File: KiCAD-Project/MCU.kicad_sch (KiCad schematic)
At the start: 35 parts, among them J301 GPIOs, J302 JTAG/SWD, J303 Conn_01x03_Shielded, U301 CY8C6244AZI-S4D92, U302 MCP9700AT-HTT, Y301 32MHz

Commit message: fixing DRC
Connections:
- net DRV_CAL: now also U301.43 (P9.4); no longer U301.48 (P10.0)
- net DRV_CS: now also U301.42 (P9.3); no longer U301.36 (P7.3)
- net DRV_MISO: now also U301.40 (P9.1); no longer U301.38 (P8.1)
- net DRV_MOSI: now also U301.39 (P9.0); no longer U301.37 (P8.0)
- net DRV_PWM_AH: now also U301.34 (P7.1); no longer U301.40 (P9.1)
- net DRV_PWM_AL: now also U301.33 (P7.0); no longer U301.39 (P9.0)
- net DRV_PWM_BH: now also U301.36 (P7.3); no longer U301.42 (P9.3)
- net DRV_PWM_BL: now also U301.35 (P7.2); no longer U301.41 (P9.2)
- net DRV_PWM_CH: now also U301.38 (P8.1); no longer U301.44 (P9.5)
- net DRV_PWM_CL: now also U301.37 (P8.0); no longer U301.43 (P9.4)
- net DRV_SCK: now also U301.41 (P9.2); no longer U301.35 (P7.2)
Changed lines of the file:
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@@
   (no_connect (at 158.75 27.94))
   (no_connect (at 158.75 33.02))
-  (no_connect (at 158.75 43.18))
-  (no_connect (at 158.75 45.72))
+  (no_connect (at 158.75 78.74))
+  (no_connect (at 158.75 83.82))
   (no_connect (at 158.75 101.6))
   (no_connect (at 339.09 148.59))
@@
     (stroke (width 0) (type solid) (color 0 0 0 0))
   )
+  (wire (pts (xy 158.75 43.18) (xy 193.04 43.18))
+    (stroke (width 0) (type solid) (color 0 0 0 0))
+  )
+  (wire (pts (xy 158.75 45.72) (xy 193.04 45.72))
+    (stroke (width 0) (type solid) (color 0 0 0 0))
+  )
   (wire (pts (xy 158.75 48.26) (xy 193.04 48.26))
     (stroke (width 0) (type solid) (color 0 0 0 0))
@@
   )
   (wire (pts (xy 158.75 76.2) (xy 193.04 76.2))
-    (stroke (width 0) (type solid) (color 0 0 0 0))
-  )
-  (wire (pts (xy 158.75 78.74) (xy 193.04 78.74))
-    (stroke (width 0) (type solid) (color 0 0 0 0))
-  )
-  (wire (pts (xy 158.75 83.82) (xy 193.04 83.82))
     (stroke (width 0) (type solid) (color 0 0 0 0))
   )
@@
     (effects (font (size 1.27 1.27)) (justify right))
   )
-  (hierarchical_label "DRV_SCK" (shape input) (at 193.04 48.26 0)
-    (effects (font (size 1.27 1.27)) (justify left))
-  )
-  (hierarchical_label "DRV_CS" (shape input) (at 193.04 50.8 0)
-    (effects (font (size 1.27 1.27)) (justify left))
-  )
-  (hierarchical_label "DRV_MOSI" (shape input) (at 193.04 58.42 0)
-    (effects (font (size 1.27 1.27)) (justify left))
-  )
-  (hierarchical_label "DRV_MISO" (shape input) (at 193.04 60.96 0)
-    (effects (font (size 1.27 1.27)) (justify left))
-  )
-  (hierarchical_label "DRV_PWM_AL" (shape input) (at 193.04 66.04 0)
-    (effects (font (size 1.27 1.27)) (justify left))
-  )
-  (hierarchical_label "DRV_PWM_AH" (shape input) (at 193.04 68.58 0)
-    (effects (font (size 1.27 1.27)) (justify left))
-  )
-  (hierarchical_label "DRV_PWM_BL" (shape input) (at 193.04 71.12 0)
-    (effects (font (size 1.27 1.27)) (justify left))
-  )
-  (hierarchical_label "DRV_PWM_BH" (shape input) (at 193.04 73.66 0)
-    (effects (font (size 1.27 1.27)) (justify left))
-  )
-  (hierarchical_label "DRV_PWM_CL" (shape input) (at 193.04 76.2 0)
-    (effects (font (size 1.27 1.27)) (justify left))
-  )
-  (hierarchical_label "DRV_PWM_CH" (shape input) (at 193.04 78.74 0)
-    (effects (font (size 1.27 1.27)) (justify left))
-  )
-  (hierarchical_label "DRV_CAL" (shape input) (at 193.04 83.82 0)
-    (effects (font (size 1.27 1.27)) (justify left))
-  )
+  (hierarchical_label "DRV_PWM_AL" (shape input) (at 193.04 43.18 0)
+    (effects (font (size 1.27 1.27)) (justify left))
+  )
+  (hierarchical_label "DRV_PWM_AH" (shape input) (at 193.04 45.72 0)
+    (effects (font (size 1.27 1.27)) (justify left))
+  )
+  (hierarchical_label "DRV_PWM_BL" (shape input) (at 193.04 48.26 0)
+    (effects (font (size 1.27 1.27)) (justify left))
+  )
+  (hierarchical_label "DRV_PWM_BH" (shape input) (at 193.04 50.8 0)
+    (effects (font (size 1.27 1.27)) (justify left))
+  )
+  (hierarchical_label "DRV_PWM_CL" (shape input) (at 193.04 58.42 0)
+    (effects (font (size 1.27 1.27)) (justify left))
+  )
+  (hierarchical_label "DRV_PWM_CH" (shape input) (at 193.04 60.96 0)
+    (effects (font (size 1.27 1.27)) (justify left))
+  )
+  (hierarchical_label "DRV_MOSI" (shape input) (at 193.04 66.04 0)
+    (effects (font (size 1.27 1.27)) (justify left))
+  )
+  (hierarchical_label "DRV_MISO" (shape input) (at 193.04 68.58 0)
+    (effects (font (size 1.27 1.27)) (justify left))
+  )
+  (hierarchical_label "DRV_SCK" (shape input) (at 193.04 71.12 0)
+    (effects (font (size 1.27 1.27)) (justify left))
+  )
+  (hierarchical_label "DRV_CS" (shape input) (at 193.04 73.66 0)
+    (effects (font (size 1.27 1.27)) (justify left))
+  )
+  (hierarchical_label "DRV_CAL" (shape input) (at 193.04 76.2 0)
+    (effects (font (size 1.27 1.27)) (justify left))
+  )

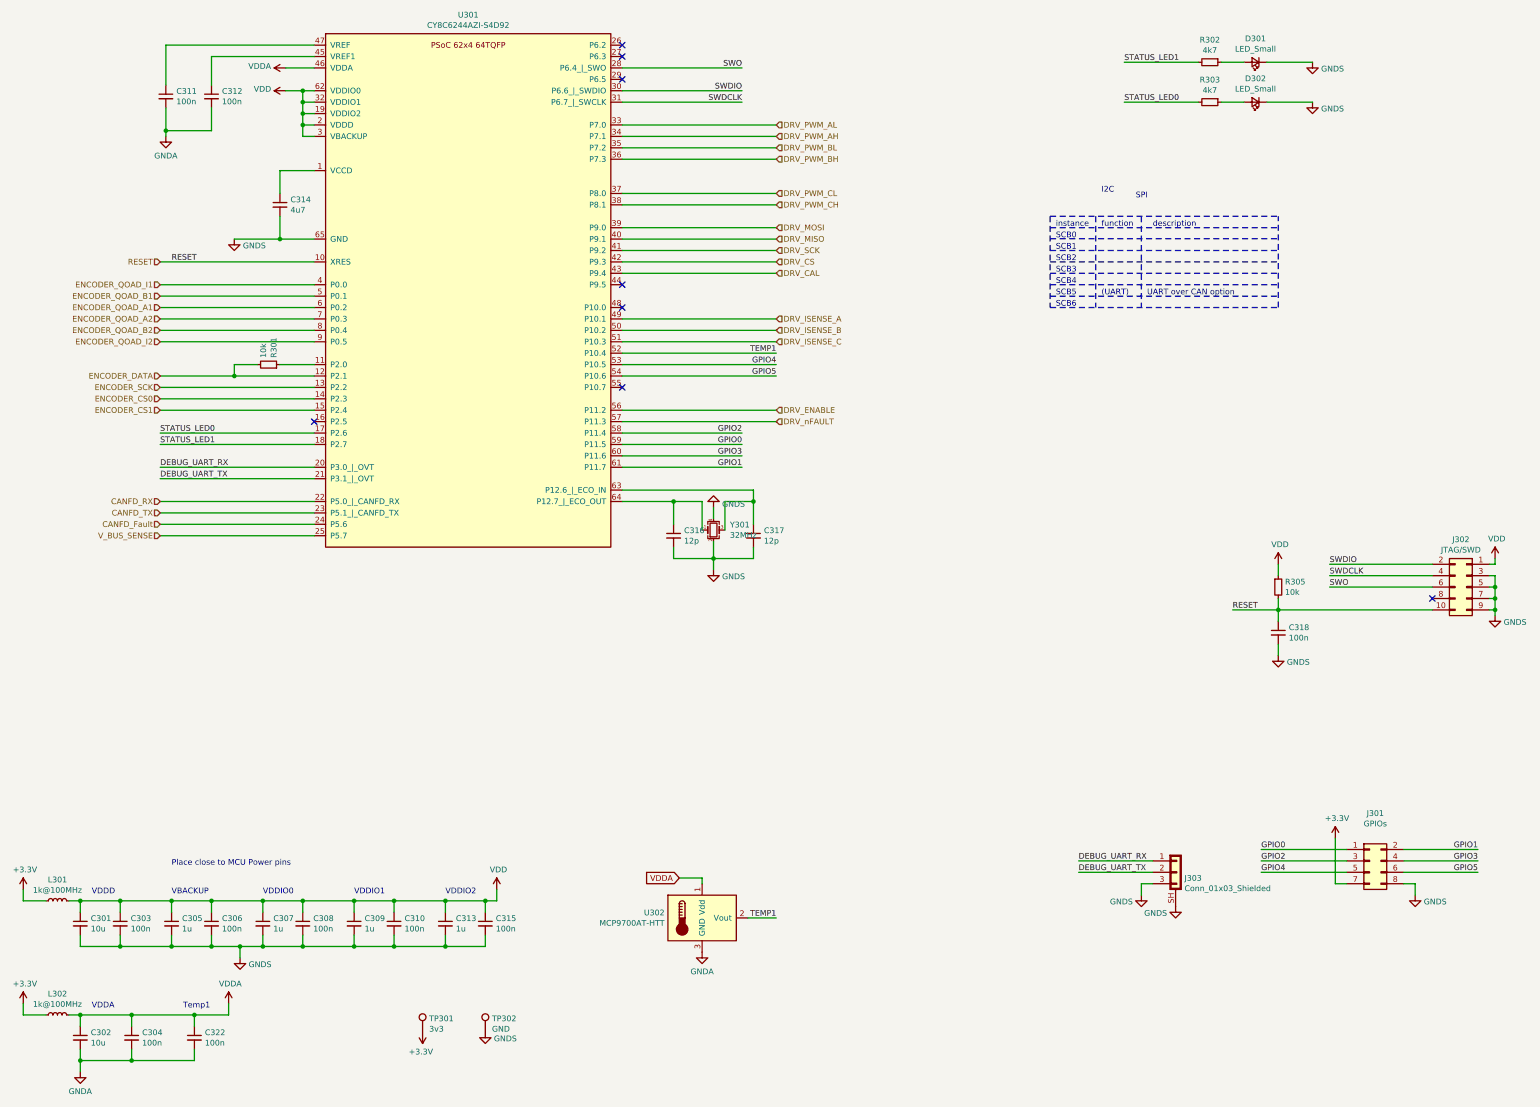
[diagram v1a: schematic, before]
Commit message: DRC resolved
removed GNDA, GNDS from schematic due to no solution was found to get a net-tie in inner layers
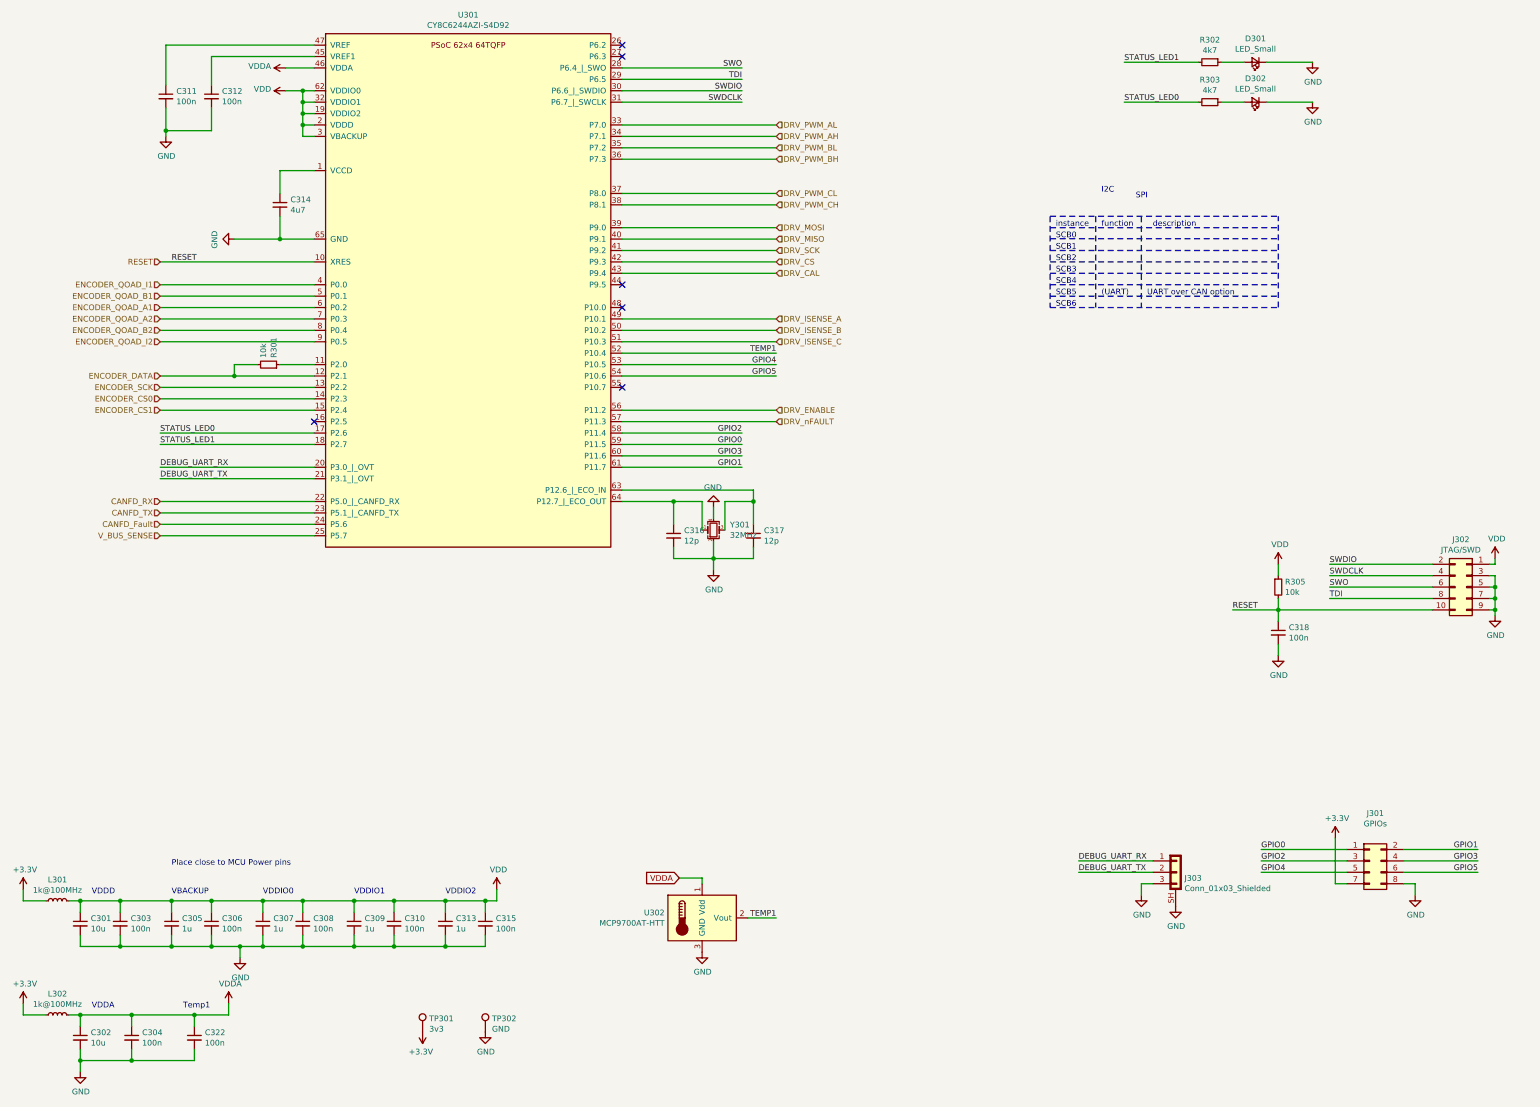
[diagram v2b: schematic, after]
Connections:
- net GNDS is gone; now on net GND: C301.2, C303.2, C305.2, C306.2, C307.2, C308.2, C309.2, C310.2, C313.2, C314.2, C315.2, C316.2, C317.2, C318.2, D301.1 (K), D302.1 (K), J301.8 (Pin_8), J302.3 (Pin_3), J302.5 (Pin_5), J302.7 (Pin_7), J302.9 (Pin_9), J303.3 (Pin_3), J303.SH (Shield), TP302.1, U301.65 (GND), Y301.2, Y301.4
- net TDI: now reaches U301.29 (P6.5)
- net TDI: now also J302.8 (Pin_8)
- net GNDA renamed GND
- no-connect marks 8 -> 6

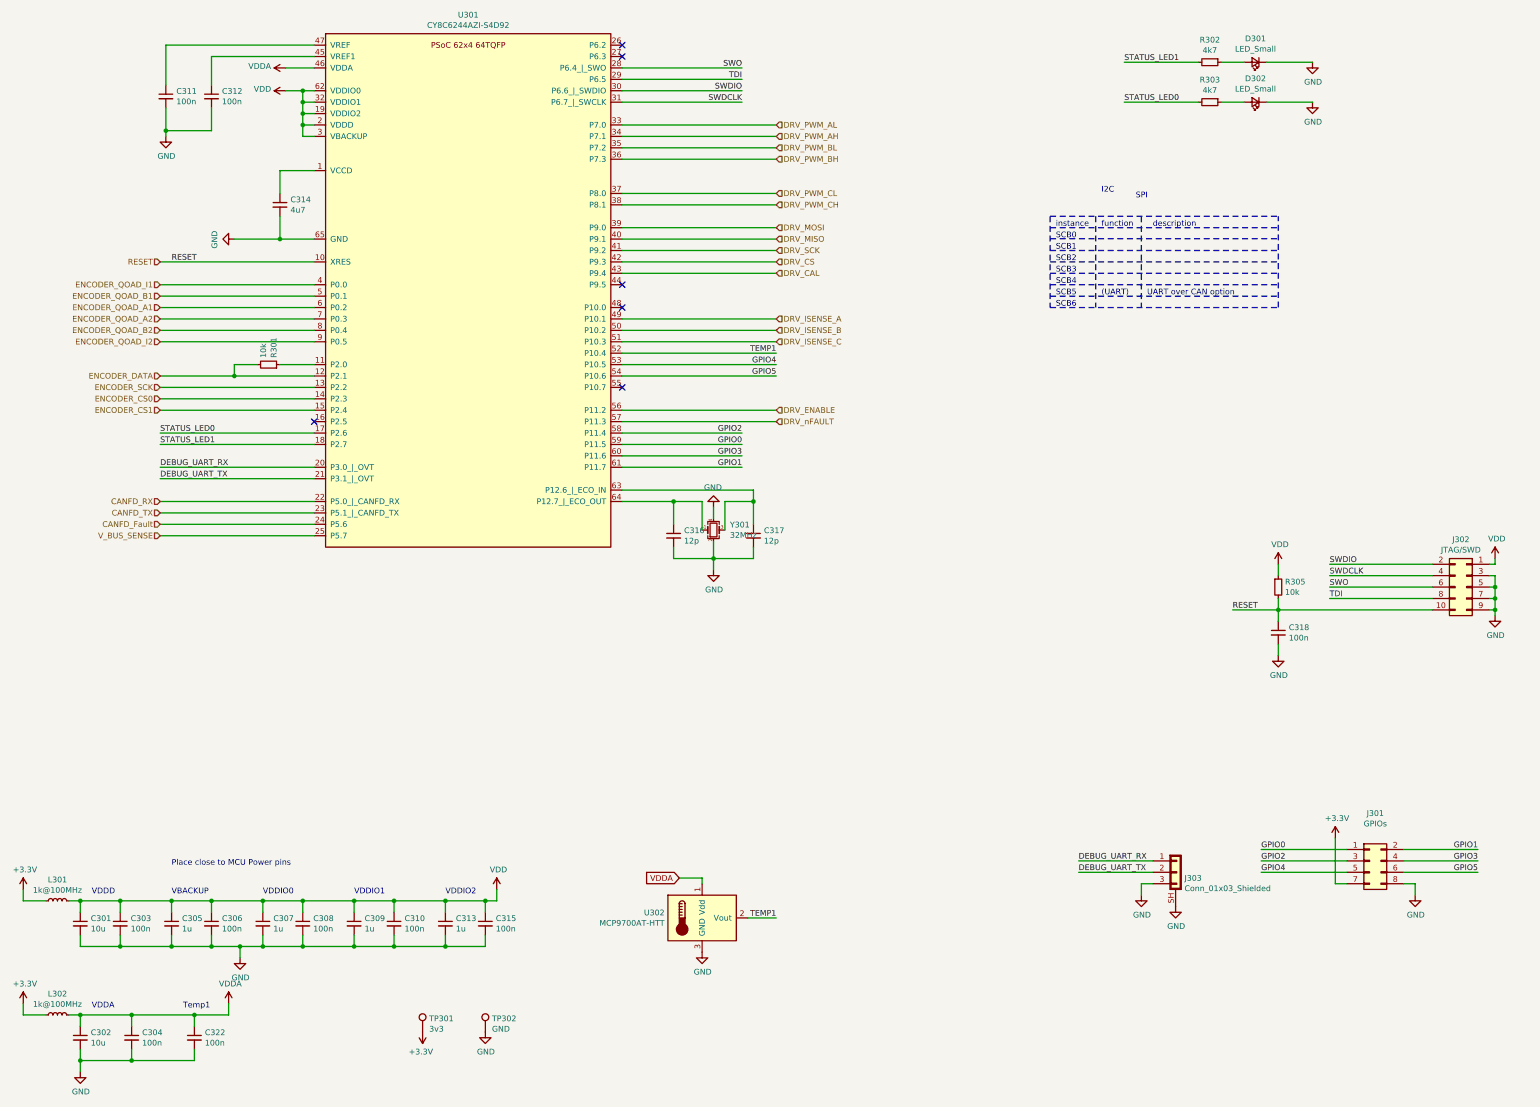
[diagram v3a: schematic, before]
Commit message: assigned debug UART to different pins
debug UART and DRV SPI used same SCB
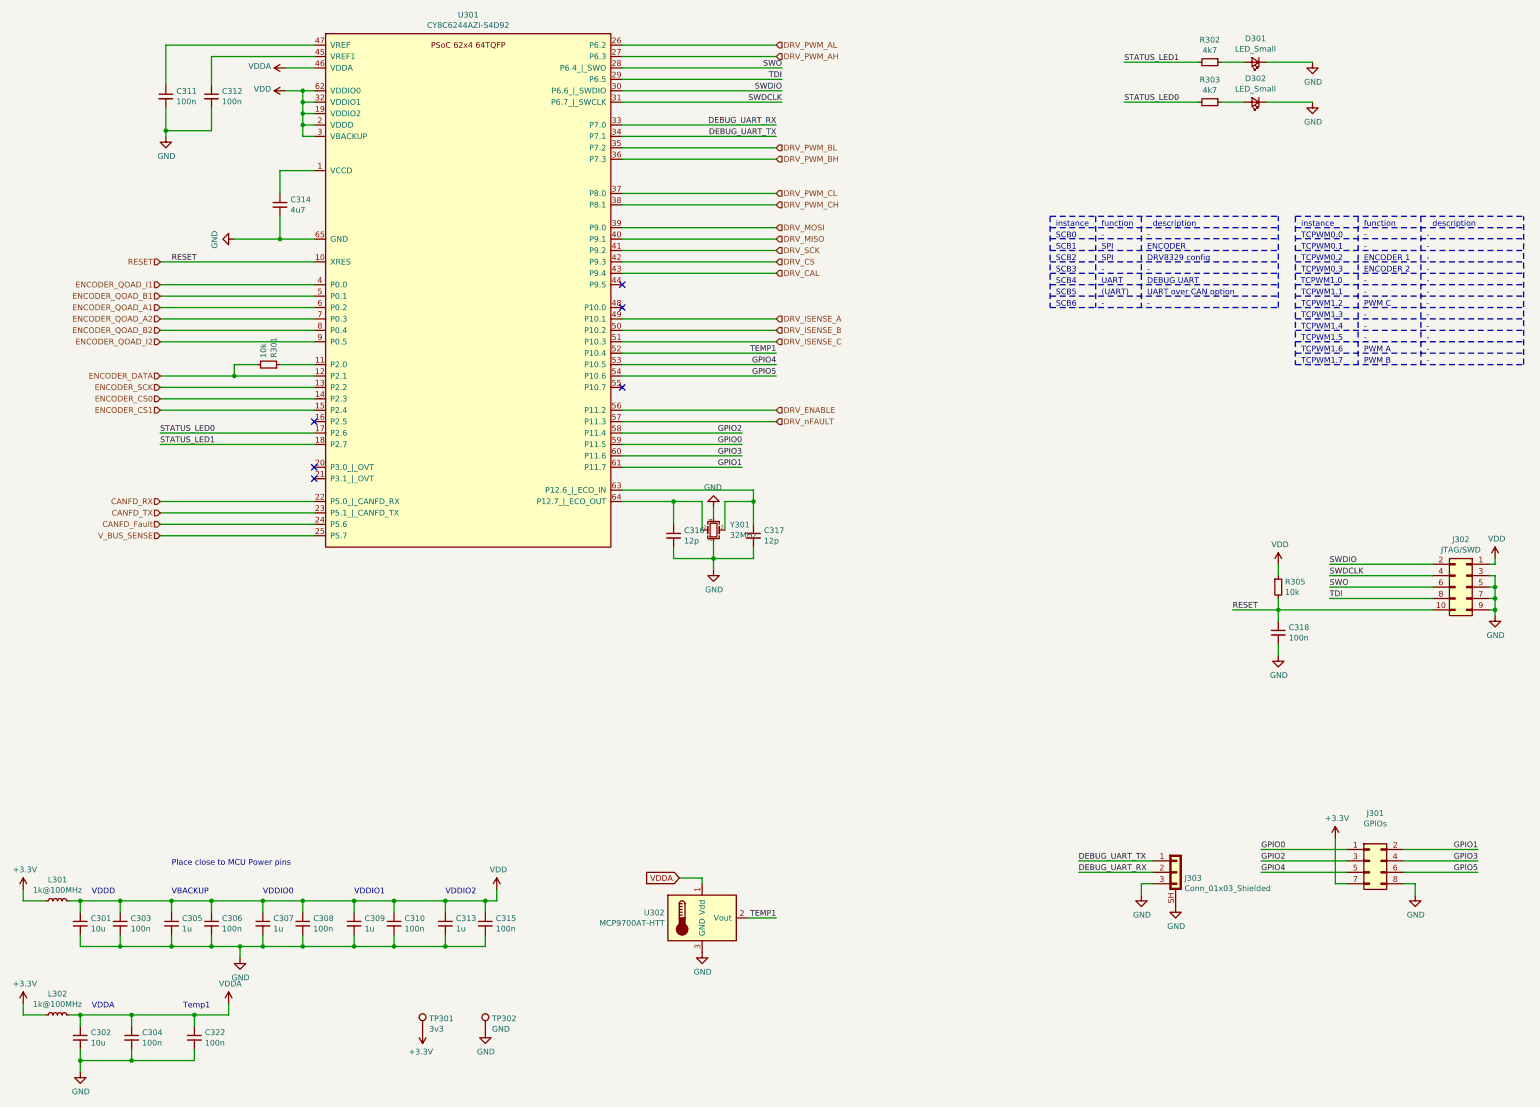
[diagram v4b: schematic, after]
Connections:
- net DEBUG_UART_RX: now also J303.2 (Pin_2), U301.33 (P7.0); no longer J303.1 (Pin_1), U301.20 (P3.0_|_OVT)
- net DEBUG_UART_TX: now also J303.1 (Pin_1), U301.34 (P7.1); no longer J303.2 (Pin_2), U301.21 (P3.1_|_OVT)
- net DRV_PWM_AH: now also U301.27 (P6.3); no longer U301.34 (P7.1)
- net DRV_PWM_AL: now also U301.26 (P6.2); no longer U301.33 (P7.0)
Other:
- note added: "-"
- note added: "DEBUG UART"
- note added: "DRV8329 config"
- note added: "ENCODER"
- note added: "ENCODER 1"
- note added: "ENCODER 2"
- note added: "PWM A"
- note added: "PWM B"
- note added: "PWM C"
- note added: "TCPWM0.0"
- note added: "TCPWM0.1"
- note added: "TCPWM0.2"
- note added: "TCPWM0.3"
- note added: "TCPWM1.0"
- note added: "TCPWM1.1"
- note added: "TCPWM1.2"
- note added: "TCPWM1.3"
- note added: "TCPWM1.4"
- note added: "TCPWM1.5"
- note added: "TCPWM1.6"
- note added: "TCPWM1.7"
- note added: "UART"
- note removed: "I2C"
